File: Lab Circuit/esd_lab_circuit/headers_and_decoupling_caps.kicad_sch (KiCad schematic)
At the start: 4 parts

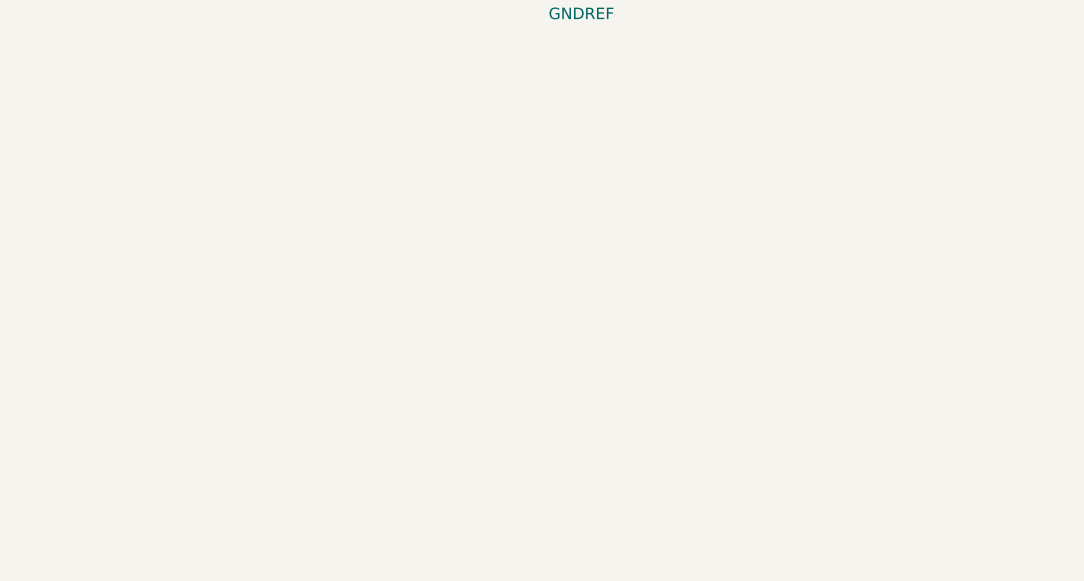
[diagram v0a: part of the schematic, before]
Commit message: Fixed the timer
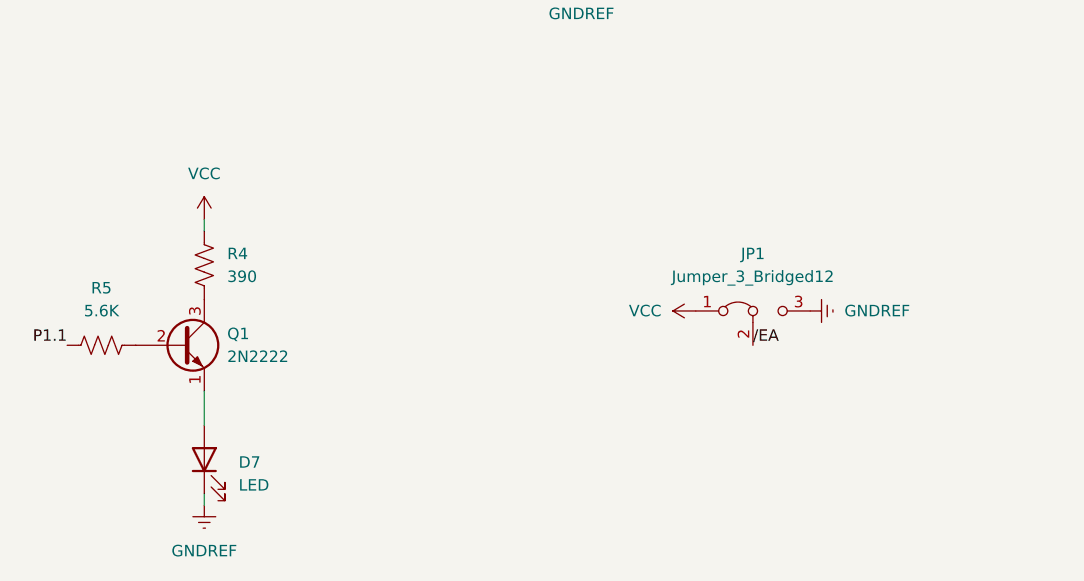
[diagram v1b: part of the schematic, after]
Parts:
- added D7: LED, symbol Device:LED
- added JP1: Jumper_3_Bridged12, symbol Jumper:Jumper_3_Bridged12
- added Q1: 2N2222, Package_TO_SOT_THT:TO-39-3, symbol ESD:2N2219
- added R4: 390, symbol Device:R_US
- added R5: 5.6K, symbol Device:R_US
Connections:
- net GNDREF: now also D7.1 (K), JP1.3 (B)
- new net: Q1.3 (C), R4.2
- new net: Q1.2 (B), R5.1
- new net: D7.2 (A), Q1.1 (E)
- new net P1.1: R5.2
- new net VCC: JP1.1 (A), R4.1
- new net /EA: JP1.2 (C)

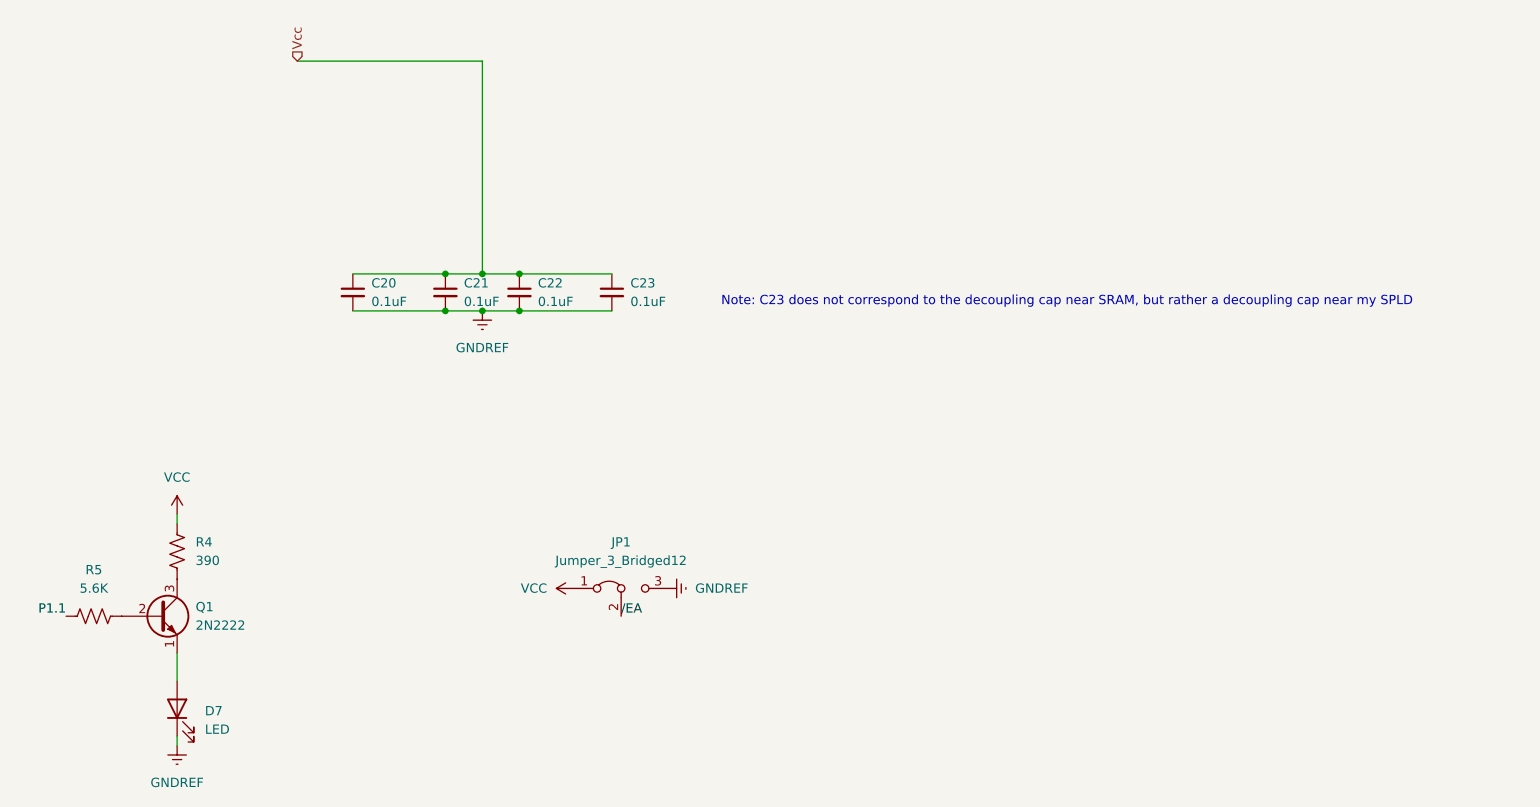
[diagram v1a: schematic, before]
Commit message: Added Debug Latch to schematic
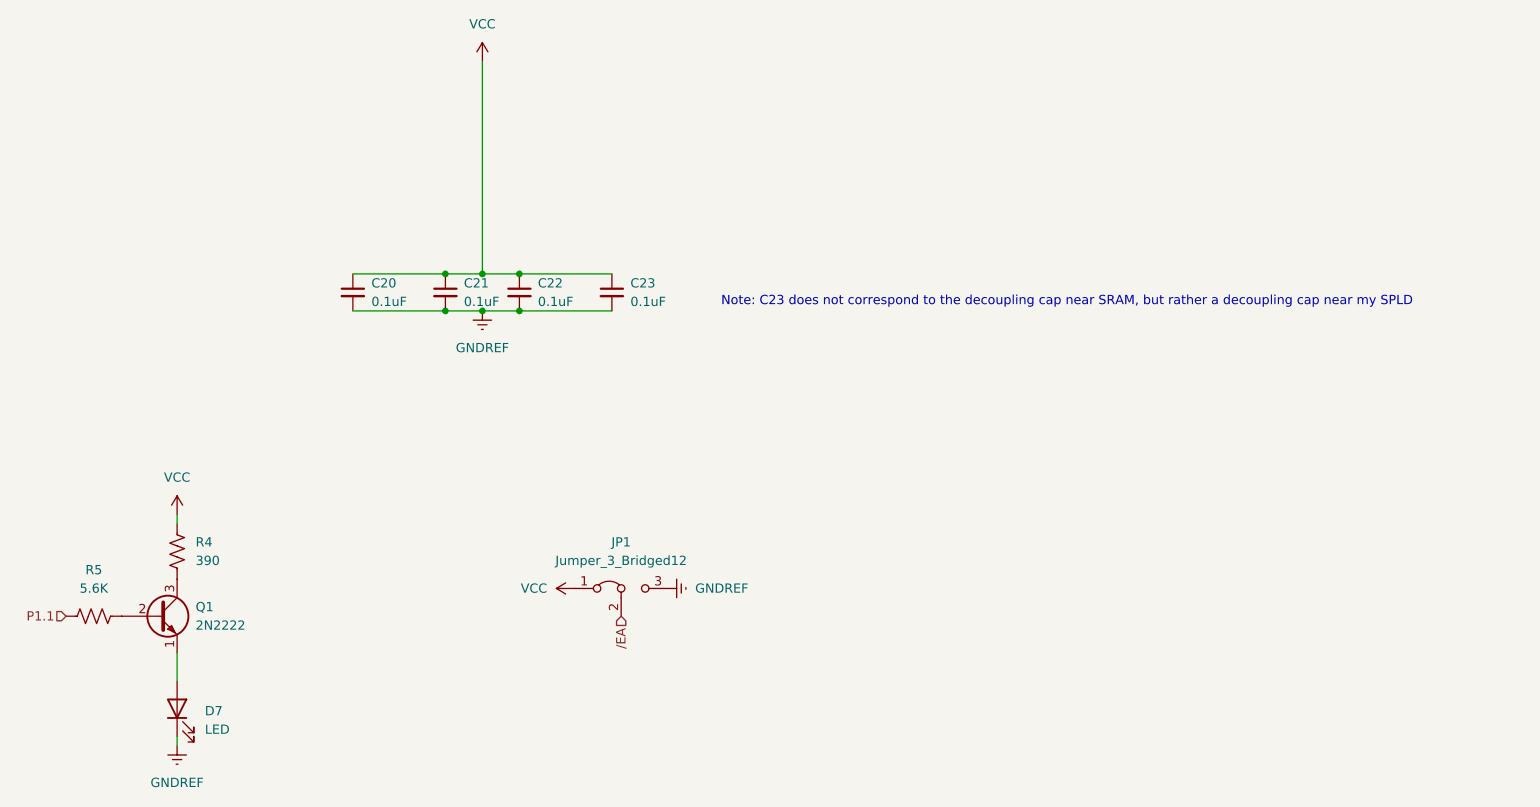
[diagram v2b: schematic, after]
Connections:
- net Vcc is gone; now on net VCC: C20.1, C21.1, C22.1, C23.1
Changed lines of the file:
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@@
 	(wire
 		(pts
-			(xy 81.28 39.37) (xy 106.68 39.37)
+			(xy 106.68 68.58) (xy 111.76 68.58)
 		)
 		(stroke
@@
 	(wire
 		(pts
-			(xy 106.68 68.58) (xy 111.76 68.58)
+			(xy 64.77 102.87) (xy 64.77 101.6)
 		)
 		(stroke
@@
 	(wire
 		(pts
-			(xy 64.77 102.87) (xy 64.77 101.6)
+			(xy 106.68 39.37) (xy 106.68 68.58)
 		)
 		(stroke
@@
 		)
 	)
-	(wire
-		(pts
-			(xy 106.68 39.37) (xy 106.68 68.58)
-		)
-		(stroke
-			(width 0)
-			(type default)
-		)
-	)
-	(label "P1.1"
+	(hierarchical_label "P1.1"
+		(shape input)
 		(at 49.53 115.57 180)
 		(effects
@@
 				(size 1.27 1.27)
 			)
-			(justify right bottom)
-		)
-	)
-	(label "{slash}EA"
-		(at 125.73 115.57 0)
+			(justify right)
+		)
+	)
+	(hierarchical_label "{slash}EA"
+		(shape input)
+		(at 125.73 115.57 270)
 		(effects
 			(font
 				(size 1.27 1.27)
 			)
-			(justify left bottom)
-		)
-	)
-	(hierarchical_label "Vcc"
-		(shape input)
-		(at 81.28 39.37 90)
-		(effects
-			(font
-				(size 1.27 1.27)
-			)
-			(justify left)
+			(justify right)
 		)
 	)
@@
 					(unit 1)
 				)
+			)
+		)
+	)
+	(symbol
+		(lib_id "power:VCC")
+		(at 106.68 39.37 0)
+		(unit 1)
+		(exclude_from_sim no)
+		(in_bom yes)
+		(on_board yes)
+		(dnp no)
+		(fields_autoplaced yes)
+		(property "Reference" "#PWR028"
+			(at 106.68 43.18 0)
+			(effects
+				(font
+					(size 1.27 1.27)
+				)
+				(hide yes)
+			)
+		)
+		(property "Value" "VCC"
+			(at 106.68 34.29 0)
+			(effects
+				(font
+					(size 1.27 1.27)
+				)
+			)
+		)
+		(property "Footprint" ""
+			(at 106.68 39.37 0)
+			(effects
+				(font
+					(size 1.27 1.27)
+				)
+				(hide yes)
+			)
+		)
+		(property "Datasheet" ""
+			(at 106.68 39.37 0)
+			(effects
+				(font
+					(size 1.27 1.27)
+				)
+				(hide yes)
+			)
+		)
+		(property "Description" "Power symbol creates a global label with name \"VCC\""
+			(at 106.68 39.37 0)
+			(effects
+				(font
+					(size 1.27 1.27)
+				)
+				(hide yes)
+			)
+		)
+		(pin "1"
+		)
+		(instances
+			(project "esd_lab_circuit"
+				(path "/e737370b-dddd-4d85-b455-d3366cc4c4a7/31d7adbf-904c-42fa-91b4-03fc269c1533"
+					(reference "#PWR028")
+					(unit 1)
+				)

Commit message: Experimental Debug Latch
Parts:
- added C12: 0.1uF, symbol Device:C_Small
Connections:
- net GNDREF: now also C12.2
- net VCC: now also C12.1
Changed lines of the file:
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@@
+	)
+	(junction
+		(at 88.9 73.66)
+		(diameter 0)
+		(color 0 0 0 0)
+	)
+	(junction
+		(at 88.9 68.58)
+		(diameter 0)
+		(color 0 0 0 0)
 	)
 	(junction
@@
 	(wire
 		(pts
+			(xy 88.9 73.66) (xy 101.6 73.66)
+		)
+		(stroke
+			(width 0)
+			(type default)
+		)
+	)
+	(wire
+		(pts
+			(xy 106.68 73.66) (xy 111.76 73.66)
+		)
+		(stroke
+			(width 0)
+			(type default)
+		)
+	)
+	(wire
+		(pts
+			(xy 64.77 120.65) (xy 64.77 124.46)
+		)
+		(stroke
+			(width 0)
+			(type default)
+		)
+	)
+	(wire
+		(pts
+			(xy 111.76 68.58) (xy 124.46 68.58)
+		)
+		(stroke
+			(width 0)
+			(type default)
+		)
+	)
+	(wire
+		(pts
+			(xy 101.6 73.66) (xy 106.68 73.66)
+		)
+		(stroke
+			(width 0)
+			(type default)
+		)
+	)
+	(wire
+		(pts
+			(xy 77.47 73.66) (xy 88.9 73.66)
+		)
+		(stroke
+			(width 0)
+			(type default)
+		)
+	)
+	(wire
+		(pts
+			(xy 101.6 68.58) (xy 106.68 68.58)
+		)
+		(stroke
+			(width 0)
+			(type default)
+		)
+	)
+	(wire
+		(pts
+			(xy 77.47 68.58) (xy 88.9 68.58)
+		)
+		(stroke
+			(width 0)
+			(type default)
+		)
+	)
+	(wire
+		(pts
+			(xy 111.76 73.66) (xy 124.46 73.66)
+		)
+		(stroke
+			(width 0)
+			(type default)
+		)
+	)
+	(wire
+		(pts
+			(xy 106.68 68.58) (xy 111.76 68.58)
+		)
+		(stroke
+			(width 0)
+			(type default)
+		)
+	)
+	(wire
+		(pts
 			(xy 88.9 68.58) (xy 101.6 68.58)
-		)
-		(stroke
-			(width 0)
-			(type default)
-		)
-	)
-	(wire
-		(pts
-			(xy 88.9 73.66) (xy 101.6 73.66)
-		)
-		(stroke
-			(width 0)
-			(type default)
-		)
-	)
-	(wire
-		(pts
-			(xy 106.68 73.66) (xy 111.76 73.66)
-		)
-		(stroke
-			(width 0)
-			(type default)
-		)
-	)
-	(wire
-		(pts
-			(xy 64.77 120.65) (xy 64.77 124.46)
-		)
-		(stroke
-			(width 0)
-			(type default)
-		)
-	)
-	(wire
-		(pts
-			(xy 111.76 68.58) (xy 124.46 68.58)
-		)
-		(stroke
-			(width 0)
-			(type default)
-		)
-	)
-	(wire
-		(pts
-			(xy 101.6 73.66) (xy 106.68 73.66)
-		)
-		(stroke
-			(width 0)
-			(type default)
-		)
-	)
-	(wire
-		(pts
-			(xy 101.6 68.58) (xy 106.68 68.58)
-		)
-		(stroke
-			(width 0)
-			(type default)
-		)
-	)
-	(wire
-		(pts
-			(xy 111.76 73.66) (xy 124.46 73.66)
-		)
-		(stroke
-			(width 0)
-			(type default)
-		)
-	)
-	(wire
-		(pts
-			(xy 106.68 68.58) (xy 111.76 68.58)
 		)
 		(stroke
@@
 		)
 	)
+	(symbol
+		(lib_id "Device:C_Small")
+		(at 77.47 71.12 0)
+		(unit 1)
+		(exclude_from_sim no)
+		(in_bom yes)
+		(on_board yes)
+		(dnp no)
+		(fields_autoplaced yes)
+		(property "Reference" "C12"
+			(at 80.01 69.8562 0)
+			(effects
+				(font
+					(size 1.27 1.27)
+				)
+				(justify left)
+			)
+		)
+		(property "Value" "0.1uF"
+			(at 80.01 72.3962 0)
+			(effects
+				(font
+					(size 1.27 1.27)
+				)
+				(justify left)
+			)
+		)
+		(property "Footprint" ""
+			(at 77.47 71.12 0)
+			(effects
+				(font
+					(size 1.27 1.27)
+				)
+				(hide yes)
+			)
+		)
+		(property "Datasheet" "~"
+			(at 77.47 71.12 0)
+			(effects
+				(font
+					(size 1.27 1.27)
+				)
+				(hide yes)
+			)
+		)
+		(property "Description" "Unpolarized capacitor, small symbol"
+			(at 77.47 71.12 0)
+			(effects
+				(font
+					(size 1.27 1.27)
+				)
+				(hide yes)
+			)
+		)
+		(pin "2"
+		)
+		(pin "1"
+		)
+		(instances
+			(project "esd_lab_circuit"
+				(path "/e737370b-dddd-4d85-b455-d3366cc4c4a7/31d7adbf-904c-42fa-91b4-03fc269c1533"
+					(reference "C12")
+					(unit 1)
+				)
+			)
+		)
+	)
